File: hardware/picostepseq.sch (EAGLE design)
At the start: 27 parts, among them J1 SJ-3523-SMT, J2 SJ-3523-SMT, SW1 LED_SWITCHSTEP, SW2 LED_SWITCHSTEP, SW3 LED_SWITCHSTEP, SW4 LED_SWITCHSTEP, SW5 LED_SWITCHSTEP, SW6 LED_SWITCHSTEP, SW7 LED_SWITCHSTEP, SW8 LED_SWITCHSTEP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

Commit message: sigh trs-a/b will kill me
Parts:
- added C1: (no value), rcl:C-EU025-025X050
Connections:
- removed net M_IN: J2.2, R3.2
- removed net M_OUT: J1.2, R1.1
- new net N$13: J1.3, R1.1
- new net N$14: J2.3, R3.2
- net +3V3: now also C1.1
- net GND: now also C1.2
- net N$1: now also J1.2; no longer J1.3
- net N$4: now also J2.2; no longer J2.3
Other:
- moved on the sheet: J1, J2
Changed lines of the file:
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@@
 <part name="GND6" library="supply1" library_urn="urn:adsk.eagle:library:371" deviceset="GND" device=""/>
 <part name="+3V4" library="supply1" library_urn="urn:adsk.eagle:library:371" deviceset="+3V3" device=""/>
+<part name="C1" library="rcl" library_urn="urn:adsk.eagle:library:334" deviceset="C-EU" device="025-025X050" package3d_urn="urn:adsk.eagle:package:23629/2"/>
+<part name="GND7" library="supply1" library_urn="urn:adsk.eagle:library:371" deviceset="GND" device=""/>
 </parts>
 <sheets>
@@
 </plain>
 <instances>
-<instance part="GND44" gate="1" x="147.32" y="63.5" smashed="yes">
-<attribute name="VALUE" x="144.78" y="60.96" size="1.778" layer="96"/>
+<instance part="GND44" gate="1" x="152.4" y="78.74" smashed="yes" rot="R270">
+<attribute name="VALUE" x="149.86" y="81.28" size="1.778" layer="96" rot="R270"/>
 </instance>
 <instance part="R1" gate="G$1" x="127" y="78.74" smashed="yes" rot="MR0">
@@
 <attribute name="VALUE" x="137.16" y="72.136" size="1.778" layer="96" rot="MR180"/>
 </instance>
-<instance part="J1" gate="G$1" x="154.94" y="73.66" smashed="yes" rot="R180">
-<attribute name="NAME" x="160.040409375" y="67.922040625" size="2.201440625" layer="95" rot="R180"/>
-<attribute name="VALUE" x="147.32" y="81.28" size="2.20203125" layer="96"/>
+<instance part="J1" gate="G$1" x="162.56" y="76.2" smashed="yes" rot="MR0">
+<attribute name="NAME" x="167.660409375" y="81.937959375" size="2.201440625" layer="95" rot="MR0"/>
+<attribute name="VALUE" x="154.94" y="68.58" size="2.20203125" layer="96" rot="MR180"/>
 </instance>
 <instance part="+3V12" gate="G$1" x="114.3" y="78.74" smashed="yes" rot="MR270">
 <attribute name="VALUE" x="114.3" y="79.756" size="1.778" layer="96" rot="MR0"/>
 </instance>
-<instance part="J2" gate="G$1" x="111.76" y="111.76" smashed="yes" rot="MR180">
-<attribute name="NAME" x="106.659590625" y="106.022040625" size="2.201440625" layer="95" rot="MR180"/>
-<attribute name="VALUE" x="119.38" y="119.38" size="2.20203125" layer="96" rot="MR0"/>
-</instance>
-<instance part="GND1" gate="1" x="119.38" y="101.6" smashed="yes">
-<attribute name="VALUE" x="116.84" y="99.06" size="1.778" layer="96"/>
+<instance part="J2" gate="G$1" x="106.68" y="114.3" smashed="yes">
+<attribute name="NAME" x="101.579590625" y="120.037959375" size="2.201440625" layer="95"/>
+<attribute name="VALUE" x="114.3" y="106.68" size="2.20203125" layer="96" rot="R180"/>
+</instance>
+<instance part="GND1" gate="1" x="116.84" y="116.84" smashed="yes" rot="R90">
+<attribute name="VALUE" x="119.38" y="114.3" size="1.778" layer="96" rot="R90"/>
 </instance>
 <instance part="U2" gate="A" x="152.4" y="109.22" smashed="yes">
@@
 <attribute name="VALUE" x="160.02" y="99.06" size="1.778" layer="96"/>
 </instance>
-<instance part="+3V1" gate="G$1" x="162.56" y="127" smashed="yes" rot="MR0">
-<attribute name="VALUE" x="163.576" y="127" size="1.778" layer="96" rot="MR90"/>
+<instance part="+3V1" gate="G$1" x="162.56" y="134.62" smashed="yes" rot="MR0">
+<attribute name="VALUE" x="163.576" y="134.62" size="1.778" layer="96" rot="MR90"/>
 </instance>
 <instance part="R4" gate="G$1" x="170.18" y="116.84" smashed="yes" rot="MR270">
@@
 <instance part="+3V4" gate="G$1" x="88.9" y="203.2" smashed="yes" rot="MR90">
 <attribute name="VALUE" x="88.9" y="202.184" size="1.778" layer="96" rot="MR180"/>
+</instance>
+<instance part="C1" gate="G$1" x="157.48" y="129.54" smashed="yes">
+<attribute name="NAME" x="159.004" y="129.921" size="1.778" layer="95"/>
+<attribute name="VALUE" x="159.004" y="124.841" size="1.778" layer="96"/>
+</instance>
+<instance part="GND7" gate="1" x="157.48" y="121.92" smashed="yes">
+<attribute name="VALUE" x="154.94" y="119.38" size="1.778" layer="96"/>
 </instance>
 </instances>
@@
 <pinref part="J1" gate="G$1" pin="1"/>
 <pinref part="GND44" gate="1" pin="GND"/>
-<wire x1="147.32" y1="66.04" x2="147.32" y2="71.12" width="0.1524" layer="91"/>
 </segment>
 <segment>
 <pinref part="J2" gate="G$1" pin="1"/>
 <pinref part="GND1" gate="1" pin="GND"/>
-<wire x1="119.38" y1="104.14" x2="119.38" y2="109.22" width="0.1524" layer="91"/>
 </segment>
 <segment>
@@
 <pinref part="GND6" gate="1" pin="GND"/>
 </segment>
+<segment>
+<pinref part="C1" gate="G$1" pin="2"/>
+<pinref part="GND7" gate="1" pin="GND"/>
+</segment>
 </net>
 <net name="+3V3" class="0">
@@
 <wire x1="162.56" y1="114.3" x2="162.56" y2="121.92" width="0.1524" layer="91"/>
 <pinref part="R4" gate="G$1" pin="1"/>
-<wire x1="162.56" y1="121.92" x2="162.56" y2="124.46" width="0.1524" layer="91"/>
+<wire x1="162.56" y1="121.92" x2="162.56" y2="129.54" width="0.1524" layer="91"/>
 <wire x1="162.56" y1="121.92" x2="170.18" y2="121.92" width="0.1524" layer="91"/>
 <junction x="162.56" y="121.92"/>
+<wire x1="162.56" y1="129.54" x2="162.56" y2="132.08" width="0.1524" layer="91"/>
+<wire x1="162.56" y1="132.08" x2="157.48" y2="132.08" width="0.1524" layer="91"/>
+<pinref part="C1" gate="G$1" pin="1"/>
 </segment>
 <segment>
@@
 </segment>
 </net>
-<net name="M_IN" class="0">
-<segment>
-<pinref part="J2" gate="G$1" pin="2"/>
-<wire x1="119.38" y1="114.3" x2="127" y2="114.3" width="0.1524" layer="91"/>
-<pinref part="R3" gate="G$1" pin="2"/>
-<label x="119.38" y="114.3" size="1.778" layer="95"/>
-</segment>
-</net>
 <net name="N$4" class="0">
 <segment>
-<pinref part="J2" gate="G$1" pin="3"/>
-<wire x1="119.38" y1="111.76" x2="127" y2="111.76" width="0.1524" layer="91"/>
 <wire x1="127" y1="111.76" x2="127" y2="106.68" width="0.1524" layer="91"/>
 <pinref part="U2" gate="A" pin="C"/>
 <wire x1="139.7" y1="106.68" x2="127" y2="106.68" width="0.1524" layer="91"/>
+<pinref part="J2" gate="G$1" pin="2"/>
+<wire x1="127" y1="111.76" x2="114.3" y2="111.76" width="0.1524" layer="91"/>
 </segment>
 </net>
@@
 </segment>
 </net>
-<net name="N$1" class="0">
-<segment>
-<pinref part="R2" gate="G$1" pin="1"/>
-<pinref part="J1" gate="G$1" pin="3"/>
-<wire x1="142.24" y1="73.66" x2="147.32" y2="73.66" width="0.1524" layer="91"/>
-</segment>
-</net>
-<net name="M_OUT" class="0">
-<segment>
-<pinref part="J1" gate="G$1" pin="2"/>
-<wire x1="147.32" y1="76.2" x2="142.24" y2="76.2" width="0.1524" layer="91"/>
-<pinref part="R1" gate="G$1" pin="1"/>
-<wire x1="142.24" y1="76.2" x2="142.24" y2="78.74" width="0.1524" layer="91"/>
-<wire x1="142.24" y1="78.74" x2="132.08" y2="78.74" width="0.1524" layer="91"/>
-<label x="134.62" y="78.74" size="1.778" layer="95"/>
-</segment>
-</net>
 <net name="SCL" class="0">
 <segment>
@@
 <wire x1="73.66" y1="160.02" x2="86.36" y2="160.02" width="0.1524" layer="91"/>
 <label x="78.74" y="160.02" size="1.778" layer="95"/>
+</segment>
+</net>
+<net name="N$1" class="0">
+<segment>
+<pinref part="J1" gate="G$1" pin="2"/>
+<pinref part="R2" gate="G$1" pin="1"/>
+<wire x1="154.94" y1="73.66" x2="142.24" y2="73.66" width="0.1524" layer="91"/>
+</segment>
+</net>
+<net name="N$13" class="0">
+<segment>
+<pinref part="J1" gate="G$1" pin="3"/>
+<wire x1="154.94" y1="76.2" x2="142.24" y2="76.2" width="0.1524" layer="91"/>
+<wire x1="142.24" y1="76.2" x2="142.24" y2="78.74" width="0.1524" layer="91"/>
+<pinref part="R1" gate="G$1" pin="1"/>
+<wire x1="142.24" y1="78.74" x2="132.08" y2="78.74" width="0.1524" layer="91"/>
+</segment>
+</net>
+<net name="N$14" class="0">
+<segment>
+<pinref part="R3" gate="G$1" pin="2"/>
+<pinref part="J2" gate="G$1" pin="3"/>
+<wire x1="127" y1="114.3" x2="114.3" y2="114.3" width="0.1524" layer="91"/>
 </segment>
 </net>
@@
 will not be understood (or retained) with this version.
 </note>
+<note version="8.4" severity="warning">
+Since Version 8.4, EAGLE supports properties for SPICE simulation.
+Probes in schematics and SPICE mapping objects found in parts and library devices
+will not be understood with this version. Update EAGLE to the latest version
+for full support of SPICE simulation.
+</note>
 </compatibility>

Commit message: update to knob
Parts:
- removed R9: 1k, rcl:R-EU_0204/7
- removed SW9: LED_SWITCHSTEP, todstuff:LED_SWITCHSTEP
- added ENC1: PEC11, adafruit_electromech:ENCODER_PLUS_SWITCH_BOURNS_PEC11
- R1: value 33 -> 10
- R2: value 10 -> 33
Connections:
- removed net LED9: R9.2, U1.GP19
- removed net N$3: R9.1, SW9.5
- removed net SW9: SW9.2, U1.GP18
- new net ROTA: ENC1.P$A, U1.GP18
- new net ROTB: ENC1.P$B, U1.GP19
- new net ROTSW: ENC1.P$1, U1.GP22
- net +3V3: now also R2.2; no longer R1.2
- net GND: now also ENC1.P$2, ENC1.P$C, ENC1.P$GND1, ENC1.P$GND2; no longer SW9.1_B, SW9.6
- net MIDI_OUT: now also R1.2; no longer R2.2
- net N$1: now also R1.1; no longer R2.1
- net N$13: now also R2.1; no longer R1.1
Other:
- moved on the sheet: R1, R2

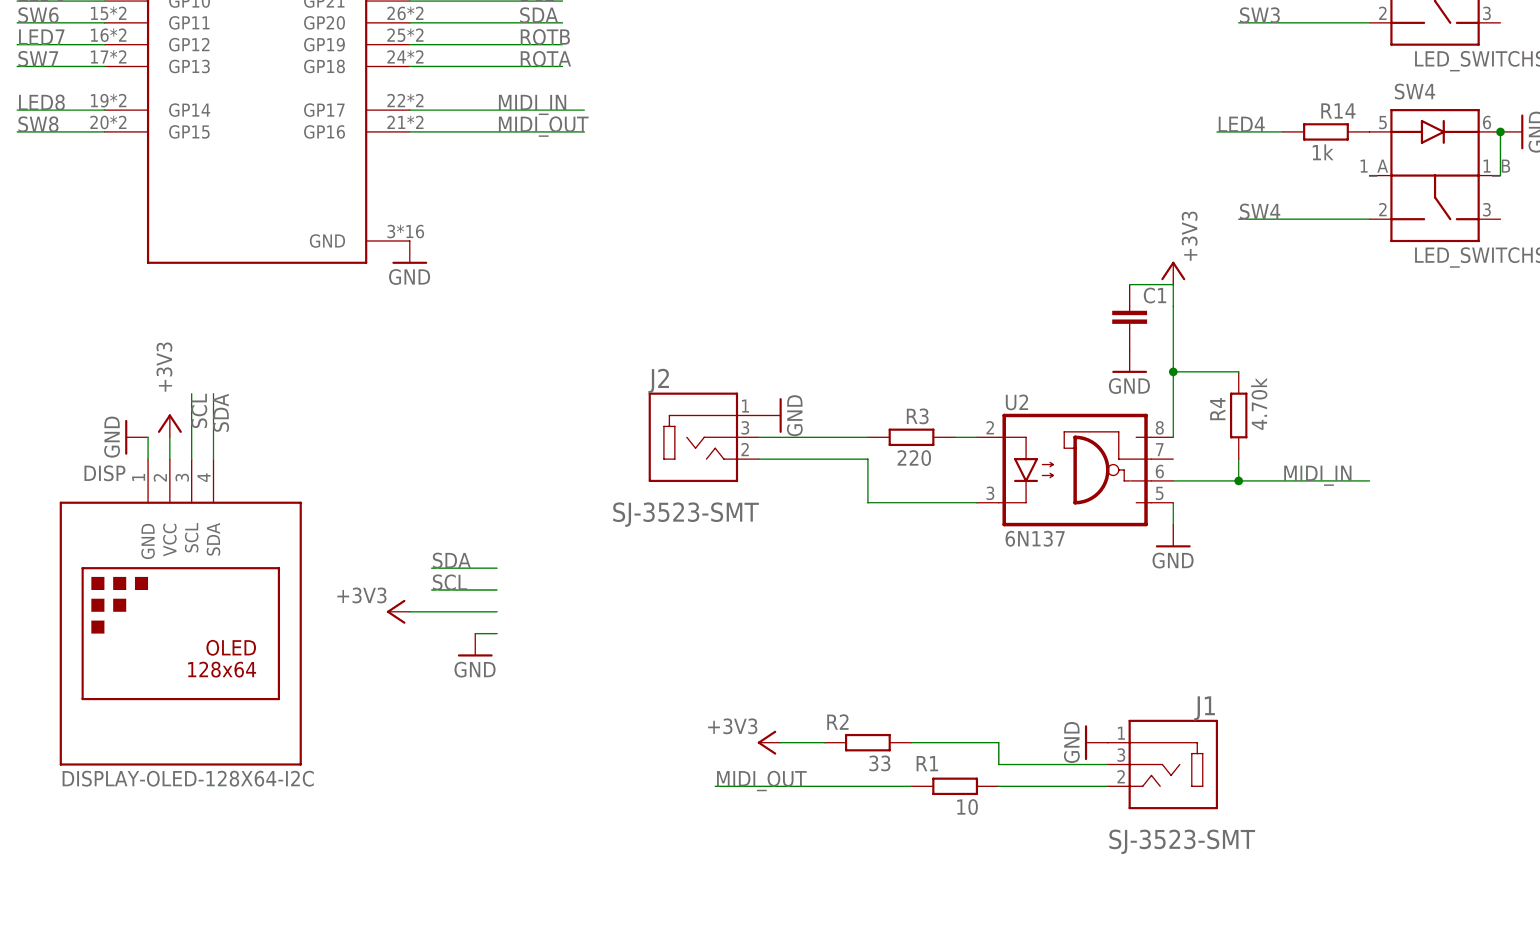
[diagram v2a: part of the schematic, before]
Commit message: move MIDI IN and MIDI OUT labels because I am dumb
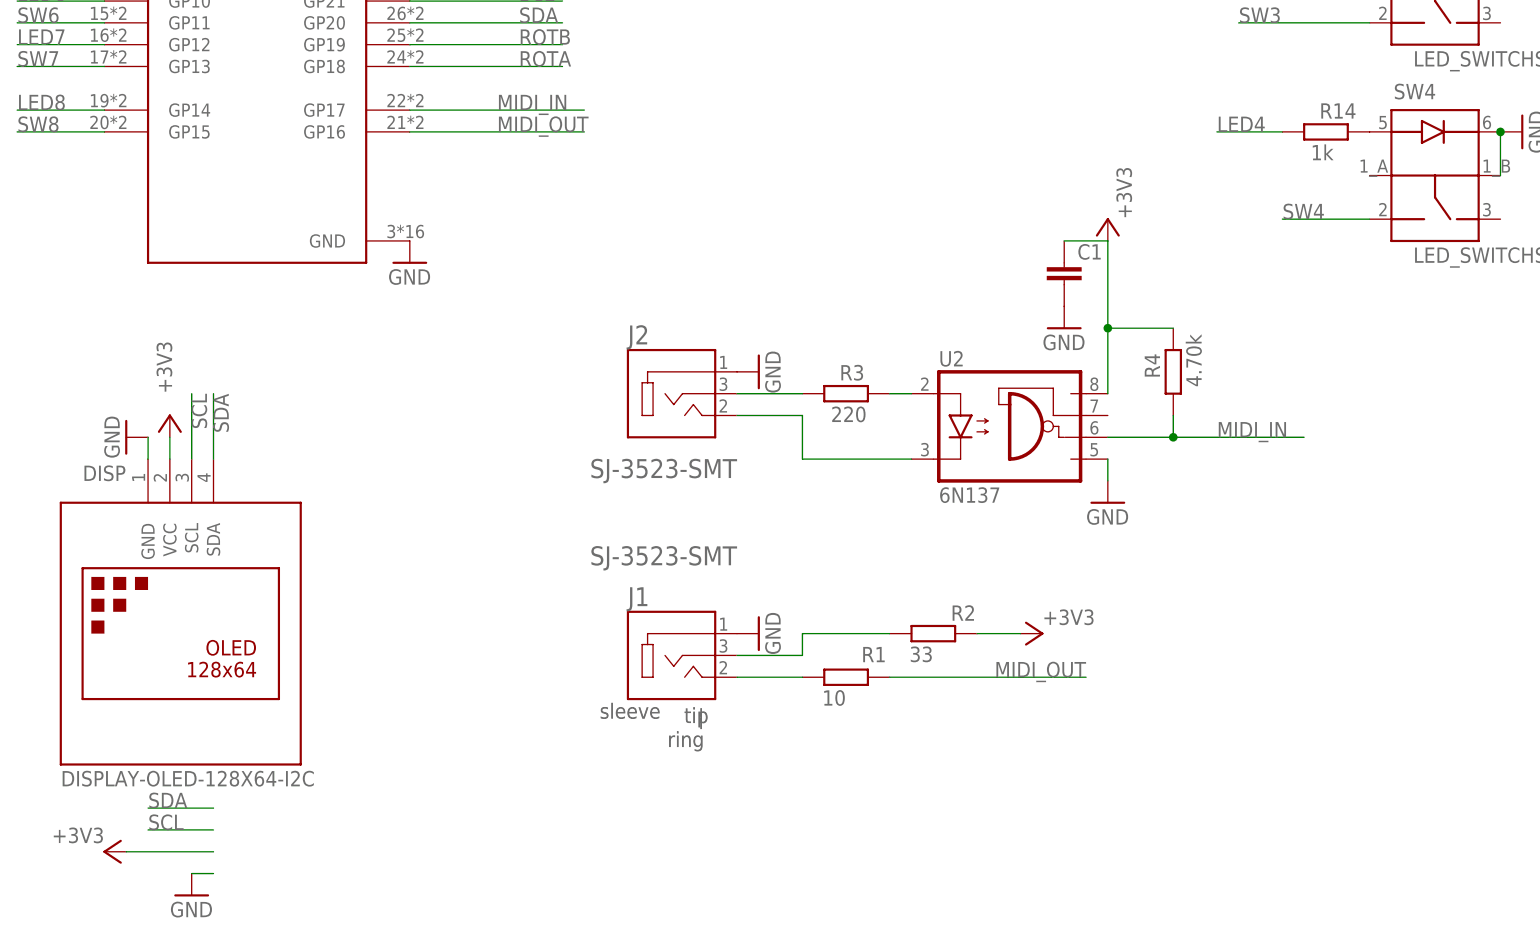
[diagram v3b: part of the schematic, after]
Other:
- note added: "sleeve"
- note added: "tip"
- note added: "| ring"
- moved on the sheet: C1, J1, J2, R1, R2, R3, R4, U2
